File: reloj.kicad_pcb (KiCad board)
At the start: 2 copper layers, 125 x 102.5 mm, 89 parts, among them J1 Conn_01x03, J2 USB_B_Mini, SW1 SW_Push, SW2 SW_Push, SW3 SW_Push, U1 LM555, U10 74LS90, U11 74LS90, U12 74LS90, U13 74LS90, U14 74LS08, U15 74LS47, U16 SA04-11SRWA, U17 74LS47, U18 SA04-11SRWA, U19 74LS47, U2 CD4060B, U20 SA04-11SRWA, U21 74LS47, U22 SA04-11SRWA, U3 74LS90, U4 74LS90, U5 74LS90, U6 74LS90, U7 74LS90, U8 74LS92, U9 74LS92, Y1 32768Hz

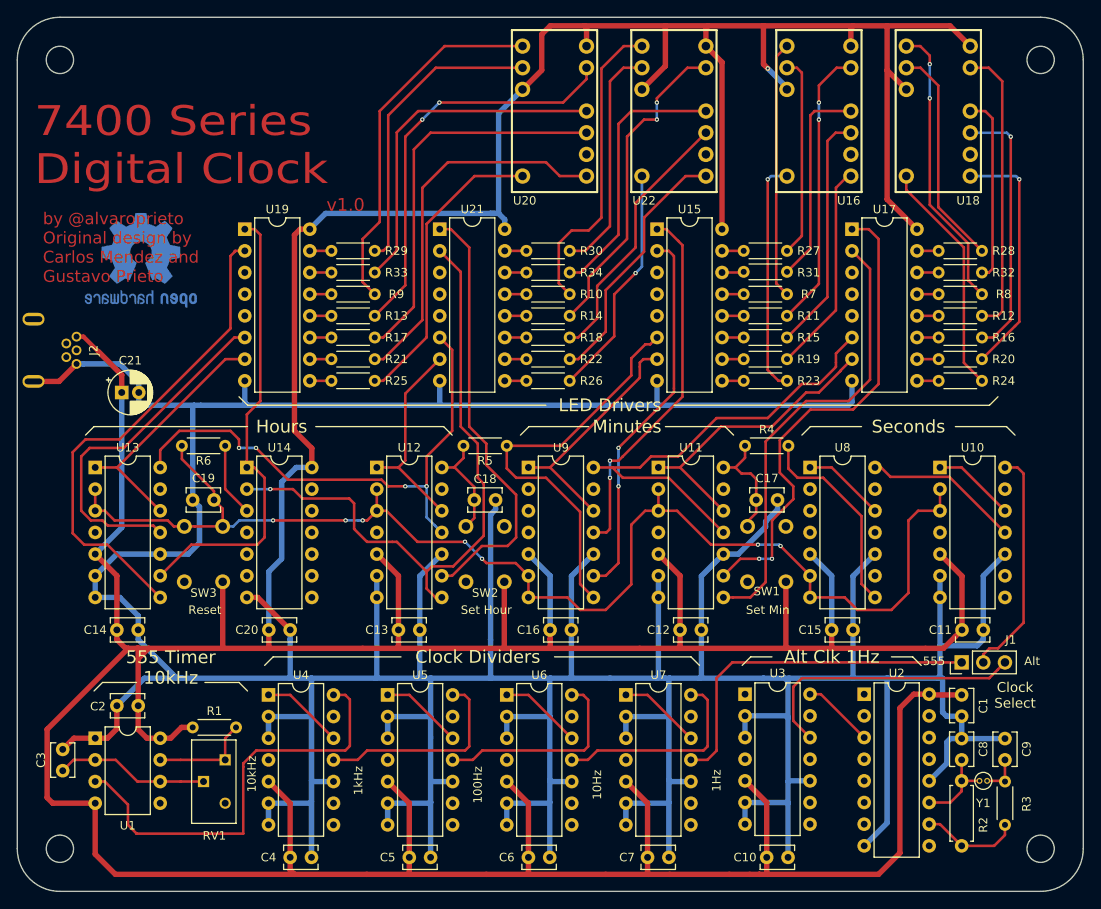
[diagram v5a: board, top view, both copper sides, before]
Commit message: Changes for v1.1
Removed global reset button.
Connected tens of minutes and tens of second counter resets to their Q3 output via RC filter. This prevents them from resetting themselves before clocking the next device.
Reduced resistor for CLK_MIN and CLK_HR so that the buttons can still overpower it.
Moved USB connector to other side and added silkscreen note
Updated reference designators to make a bit more sense

NOTE: New resistor values aren't final
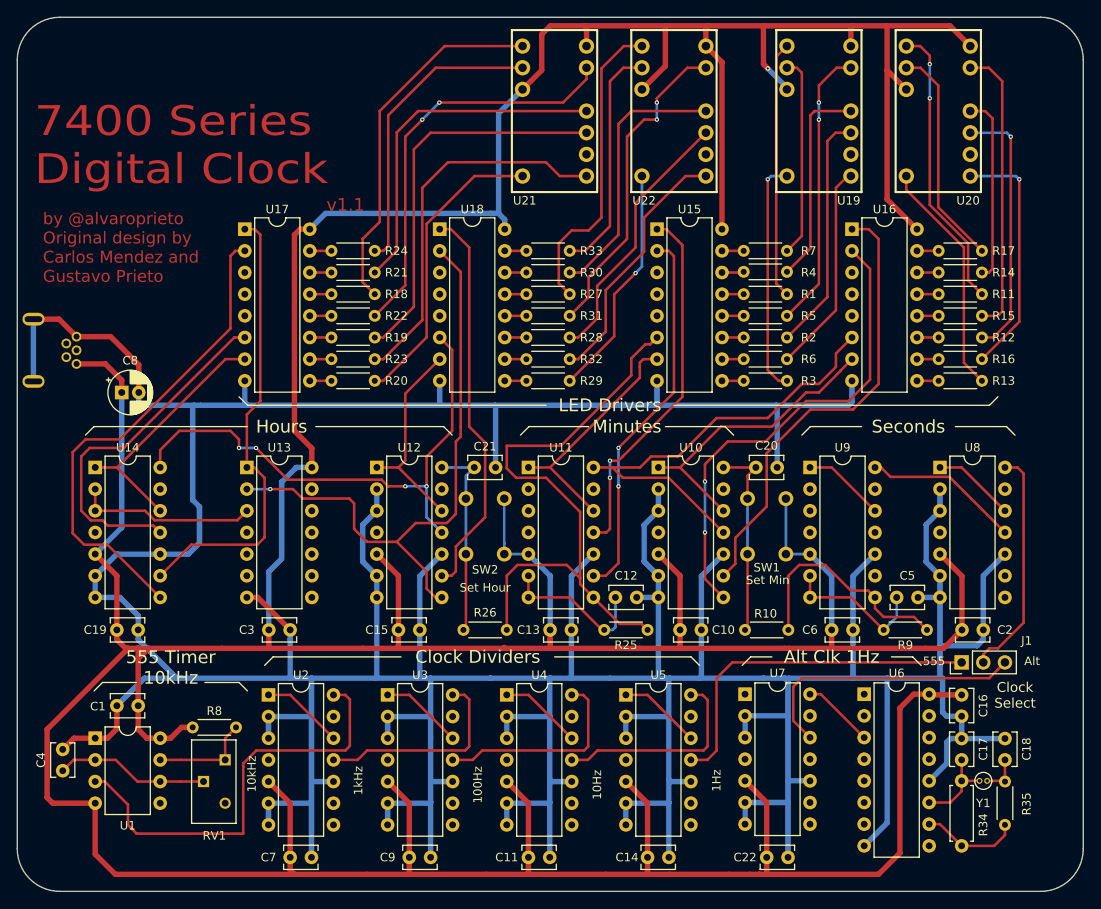
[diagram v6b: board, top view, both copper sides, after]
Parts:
- removed the C17 at (181.7, 101.6)
- removed the C19 at (118.1, 101.6)
- removed the R4 at (180.3, 95.2)
- removed the R5 at (147.3, 95.2)
- removed the R6 at (114.3, 95.2)
- removed REF**: OSHW-Logo2_14.6x12mm_Copper, Symbol:OSHW-Logo2_14.6x12mm_Copper
- removed REF** (x4): MountingHole_3.2mm_M3, MountingHole:MountingHole_3.2mm_M3
- removed SW3: SW_Push, alvarop:TE_1825910-6
- removed the U20 at (158.0, 56.0)
- added C10: 0.1u, Capacitor_THT:C_Disc_D3.8mm_W2.6mm_P2.50mm, F.Cu at (172.7, 116.8)
- added C20: 0.1u, Capacitor_THT:C_Disc_D3.8mm_W2.6mm_P2.50mm, F.Cu at (181.6, 97.8)
- added C5: 0.1u, Capacitor_THT:C_Disc_D3.8mm_W2.6mm_P2.50mm, F.Cu at (198.1, 113.0)
- added R10: 330, Resistor_THT:R_Axial_DIN0204_L3.6mm_D1.6mm_P5.08mm_Horizontal, F.Cu at (185.4, 116.8)
- added R25: 330, Resistor_THT:R_Axial_DIN0204_L3.6mm_D1.6mm_P5.08mm_Horizontal, F.Cu at (163.8, 116.8)
- added R26: 330, Resistor_THT:R_Axial_DIN0204_L3.6mm_D1.6mm_P5.08mm_Horizontal, F.Cu at (152.4, 116.8)
- added R9: 330, Resistor_THT:R_Axial_DIN0204_L3.6mm_D1.6mm_P5.08mm_Horizontal, F.Cu at (196.6, 116.8)
- added U21: SA04-11SRWA, alvarop:SA04-11SRWA, F.Cu at (158.0, 56.0)
- J2: moved to B.Cu
- moved C12 8.48 mm to (165.1, 113.0)
- moved C21 3.81 mm to (148.6, 97.8)
- moved SW1 3.25 mm to (182.9, 104.7), turned to 270 degrees
- moved SW2 3.25 mm to (149.9, 104.7), turned to 270 degrees
- turned J2 to 90 degrees
- renumbered C2 to C1, C6 to C11, C16 to C13, C7 to C14, C13 to C15, C1 to C16, C8 to C17, C9 to C18, C14 to C19, C11 to C2, C18 to C21, C10 to C22, C20 to C3, C3 to C4, C15 to C6, C4 to C7, C21 to C8, C5 to C9, R7 to R1, R8 to R11, R16 to R12, R24 to R13, R32 to R14, R12 to R15, R20 to R16, R28 to R17, R9 to R18, R17 to R19, R15 to R2, R25 to R20, R33 to R21, R13 to R22, R21 to R23, R29 to R24, R10 to R27, R18 to R28, R26 to R29, R23 to R3, R34 to R30, R14 to R31, R22 to R32, R30 to R33, R2 to R34, R3 to R35, R31 to R4, R11 to R5, R19 to R6, R27 to R7, R1 to R8, U11 to U10, U9 to U11, U14 to U13, U13 to U14, U17 to U16, U19 to U17, U21 to U18, U16 to U19, U4 to U2, U18 to U20, U5 to U3, U6 to U4, U7 to U5, U2 to U6, U3 to U7, U10 to U8, U8 to U9
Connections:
- C12 pad 1: CA -> /M_RST
- U10 pad 2: /T_RST -> GND
- U10 pad 3: /T_RST -> GND
- U11 pad 6: /T_RST -> /M_RST
- U11 pad 7: /T_RST -> /M_RST
- U12 pad 2: /T_RST -> GND
- U12 pad 3: /T_RST -> GND
- U13 pad 3: Net-(R6-Pad2) (its old number) -> /H_RST
- U14 pad 2: /T_RST -> /H_RST
- U14 pad 3: /T_RST -> /H_RST
- U8 pad 2: /T_RST -> GND
- U8 pad 3: /T_RST -> GND
- U9 pad 6: /T_RST -> /S_RST
- U9 pad 7: /T_RST -> /S_RST
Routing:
- net /T_RST: track 153.5 -> 0.00 mm, vias 7 -> 0
- net GND: track 664.1 -> 697.2 mm
- net /DM_Q3: track 48.1 -> 72.1 mm
- net /H_RST: track 0.00 -> 21.2 mm
- net /M_RST: track 0.00 -> 17.9 mm
- net /S_RST: track 0.00 -> 17.2 mm
- net /CLK_MIN: track 12.8 -> 23.4 mm
- net /CLK_HR: track 12.8 -> 23.3 mm
- net Net-(R6-Pad2) (its old number): track 8.67 -> 0.00 mm
- net CA: track 686.6 -> 680.2 mm
- net /H_Q1: track 51.2 -> 46.4 mm
- net /H_Q2: track 75.0 -> 71.4 mm
- net /M_Q1: track 57.0 -> 53.6 mm, vias 2 -> 0
- net Net-(R10-Pad1): track 23.7 -> 27.0 mm
- net /M_Q2: track 53.4 -> 56.0 mm, vias 0 -> 2
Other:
- board text added: "USB HERE"
- board text added: "v1.1"
- board text removed: "Reset"
- board text removed: "v1.0"

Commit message: Forgot to commit changed netlists
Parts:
- renumbered C18 to C10, C2 to C11, C15 to C13, C19 to C14, C5 to C15, C6 to C16, C10 to C17, C13 to C18, C20 to C19, C16 to C2, C21 to C20, C3 to C21, C8 to C22, C4 to C3, C7 to C4, C9 to C5, C11 to C6, C14 to C7, C22 to C8, C17 to C9, R8 to R1, R18 to R10, R27 to R11, R5 to R12, R15 to R13, R22 to R14, R31 to R15, R2 to R16, R12 to R17, R19 to R18, R28 to R19, R34 to R2, R6 to R20, R16 to R21, R23 to R22, R32 to R23, R3 to R24, R13 to R25, R20 to R26, R29 to R27, R7 to R28, R17 to R29, R35 to R3, R24 to R30, R33 to R31, R4 to R32, R14 to R33, R21 to R34, R30 to R35, R10 to R4, R26 to R5, R9 to R6, R25 to R7, R1 to R8, R11 to R9

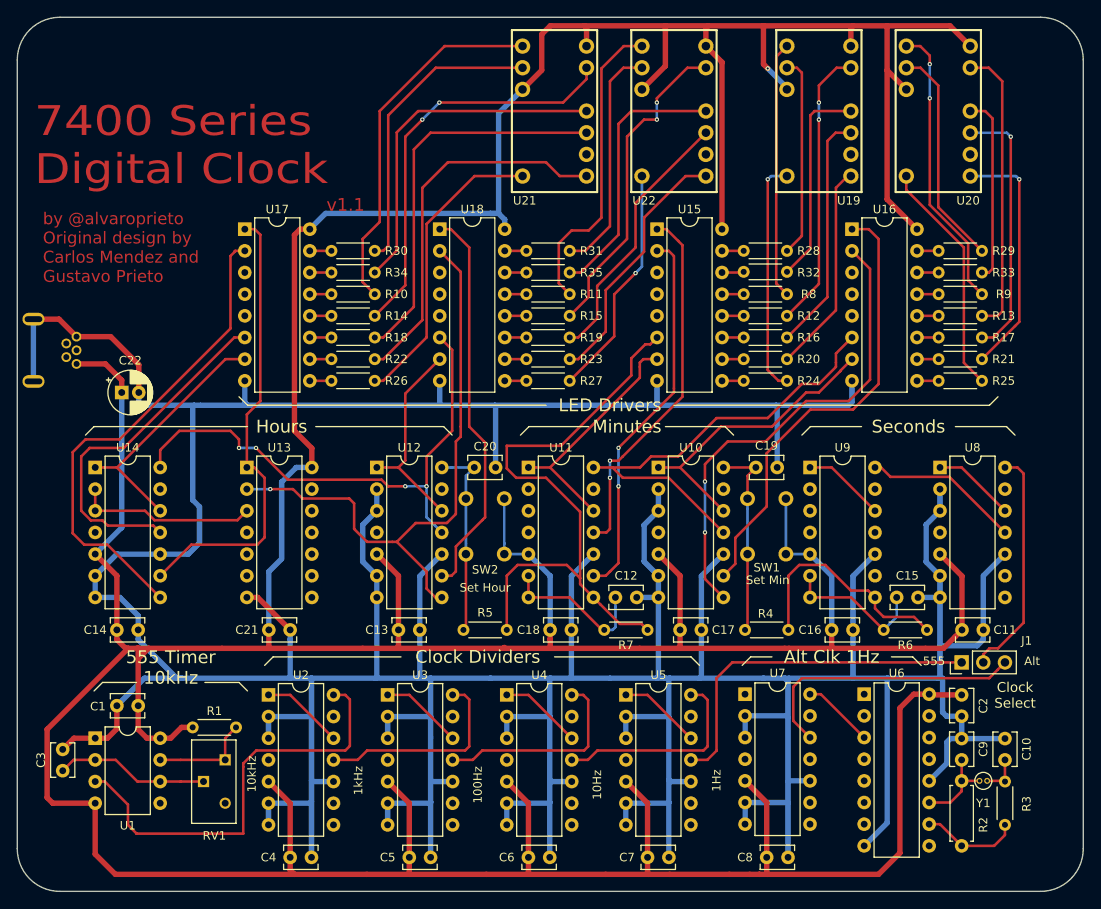
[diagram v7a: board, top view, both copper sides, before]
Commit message: Minor updates to v1.1
Updated 22pf cap BOM item
Re-added mounting holes
Polished a few traces

Sent out to Bay Area Circuits
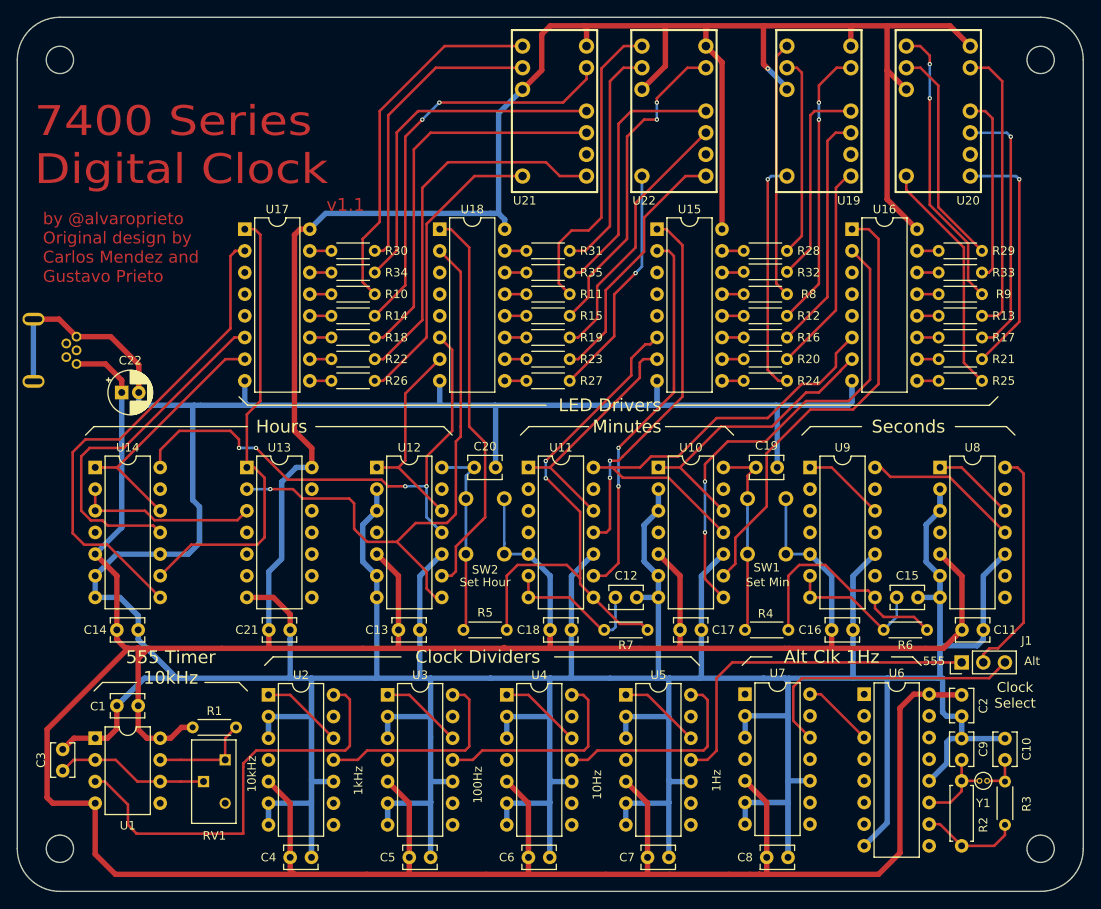
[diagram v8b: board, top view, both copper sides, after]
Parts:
- added REF**: MountingHole_3.2mm_M3, MountingHole:MountingHole_3.2mm_M3, F.Cu at (100.0, 142.5)
- added REF**: MountingHole_3.2mm_M3, MountingHole:MountingHole_3.2mm_M3, F.Cu at (100.0, 50.0)
- added REF**: MountingHole_3.2mm_M3, MountingHole:MountingHole_3.2mm_M3, F.Cu at (215.0, 50.0)
- added REF**: MountingHole_3.2mm_M3, MountingHole:MountingHole_3.2mm_M3, F.Cu at (215.0, 142.5)
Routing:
- net /DM_Q3: track 72.1 -> 62.6 mm, vias 0 -> 2
- net GND: track 697.2 -> 698.3 mm
